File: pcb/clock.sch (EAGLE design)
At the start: 50 parts, among them K1 JS-M1-9V-4, K2 JS-M1-9V-4, Q1 BC447, Q2 BC447, Q3 BC447, Q4 BC447, Q5 BC447, Q6 BC447, Q8 CSM-7X-DU, Q9 MC-306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

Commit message: some small things
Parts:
- added C2: (no value), rcl:C-EUC1206
- added C7: (no value), rcl:C-EU025-040X050
- added D1: (no value), diode:DIODE-SOD80C
- added R23: (no value), rcl:R-EU_R1206
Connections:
- new net N$66: C2.2, U1.AREF
- new net N$67: D1.C, D2.C, R23.2
- new net N$68: R23.1, U2.VDD
- net GND: now also C2.1, C7.2
- net VCC: now also C7.1, D1.A, U1.AVCC; no longer D2.C, U2.VDD
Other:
- moved on the sheet: K1, K2, Q5, Q6, Q9, R19, R20, U2, X1-2, X2-1, X2-2, X2-3

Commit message: extend board
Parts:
- removed C4: (no value), rcl:C-EUC1206
- added C6: (no value), rcl:C-EUC0805K
- C3: device rcl:C-EUC1206 -> rcl:C-EUC0805K
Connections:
- net GND: now also C6.1; no longer C4.1
- net N$30: now also C6.2; no longer C3.2
- net N$31: now also C3.2; no longer C4.2
- net N$35: now also JP3.3
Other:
- moved on the sheet: C3
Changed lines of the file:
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@@
 <setting verticaltext="up"/>
 </settings>
-<grid distance="0.1" unitdist="inch" unit="inch" style="lines" multiple="1" display="no" altdistance="0.01" altunitdist="inch" altunit="inch"/>
+<grid distance="25" unitdist="mil" unit="mil" style="lines" multiple="1" display="no" altdistance="0.01" altunitdist="inch" altunit="inch"/>
 <layers>
 <layer number="1" name="Top" color="4" fill="1" visible="no" active="no"/>
@@
 <part name="SUPPLY10" library="supply2" deviceset="VCC" device=""/>
 <part name="U$1" library="display-kingbright" deviceset="4DIGITS-7SEGMENT-C" device=""/>
-<part name="C3" library="rcl" deviceset="C-EU" device="C1206"/>
-<part name="C4" library="rcl" deviceset="C-EU" device="C1206"/>
 <part name="GND6" library="supply1" deviceset="GND" device=""/>
 <part name="GND7" library="supply1" deviceset="GND" device=""/>
@@
 <part name="D1" library="diode" deviceset="DIODE-" device="SOD80C"/>
 <part name="R23" library="rcl" deviceset="R-EU_" device="R1206"/>
+<part name="C6" library="rcl" deviceset="C-EU" device="C0805K"/>
+<part name="C3" library="rcl" deviceset="C-EU" device="C0805K"/>
 </parts>
 <sheets>
@@
 <instance part="SUPPLY10" gate="G$1" x="106.045" y="121.285"/>
 <instance part="U$1" gate="A" x="215.9" y="99.06"/>
-<instance part="C3" gate="G$1" x="38.1" y="43.18" rot="R90"/>
-<instance part="C4" gate="G$1" x="38.1" y="38.1" rot="R90"/>
 <instance part="GND6" gate="1" x="35.56" y="27.94"/>
 <instance part="GND7" gate="1" x="145.415" y="-4.445"/>
@@
 <instance part="D1" gate="G$1" x="118.745" y="115.57" rot="R270"/>
 <instance part="R23" gate="G$1" x="131.445" y="109.855" rot="R180"/>
+<instance part="C6" gate="G$1" x="38.1" y="43.18" rot="R90"/>
+<instance part="C3" gate="G$1" x="38.1" y="38.1" rot="R90"/>
 </instances>
 <busses>
@@
 </segment>
 <segment>
-<pinref part="C3" gate="G$1" pin="1"/>
-<pinref part="C4" gate="G$1" pin="1"/>
-<wire x1="35.56" y1="43.18" x2="35.56" y2="38.1" width="0.1524" layer="91"/>
 <pinref part="GND6" gate="1" pin="GND"/>
 <wire x1="35.56" y1="30.48" x2="35.56" y2="38.1" width="0.1524" layer="91"/>
+<pinref part="C6" gate="G$1" pin="1"/>
+<pinref part="C3" gate="G$1" pin="1"/>
+<wire x1="35.56" y1="38.1" x2="35.56" y2="43.18" width="0.1524" layer="91"/>
 <junction x="35.56" y="38.1"/>
 </segment>
@@
 <pinref part="U1" gate="A" pin="PB6"/>
 <wire x1="48.26" y1="43.18" x2="45.085" y2="43.18" width="0.1524" layer="91"/>
-<pinref part="C3" gate="G$1" pin="2"/>
 <pinref part="Q8" gate="P" pin="2"/>
 <wire x1="45.085" y1="43.18" x2="43.18" y2="43.18" width="0.1524" layer="91"/>
 <junction x="45.085" y="43.18"/>
+<pinref part="C6" gate="G$1" pin="2"/>
 </segment>
 </net>
@@
 <wire x1="48.26" y1="40.64" x2="48.26" y2="38.1" width="0.1524" layer="91"/>
 <wire x1="48.26" y1="38.1" x2="45.085" y2="38.1" width="0.1524" layer="91"/>
-<pinref part="C4" gate="G$1" pin="2"/>
 <pinref part="Q8" gate="P" pin="1"/>
 <wire x1="45.085" y1="38.1" x2="43.18" y2="38.1" width="0.1524" layer="91"/>
 <junction x="45.085" y="38.1"/>
+<pinref part="C3" gate="G$1" pin="2"/>
 </segment>
 </net>
@@
 <pinref part="R7" gate="G$1" pin="1"/>
 <wire x1="137.795" y1="58.42" x2="167.64" y2="58.42" width="0.1524" layer="91"/>
-</segment>
-</net>
+<pinref part="JP3" gate="A" pin="3"/>
+<wire x1="118.745" y1="58.42" x2="137.795" y2="58.42" width="0.1524" layer="91"/>
+<junction x="137.795" y="58.42"/>
+</segment>
+</net>

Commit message: temp stable version
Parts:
- removed D1: (no value), diode:DIODE-SOD80C
- removed R23: (no value), rcl:R-EU_R1206
- added D3: ES2D, diode:ES2D
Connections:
- removed net N$68: R23.1, U2.VDD
- net N$67: now also D3.C, U2.VDD; no longer D1.C, R23.2
- net VCC: now also D3.A; no longer D1.A
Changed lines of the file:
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@@
 <part name="GND22" library="supply1" deviceset="GND" device=""/>
 <part name="C7" library="rcl" deviceset="C-EU" device="025-040X050"/>
-<part name="D1" library="diode" deviceset="DIODE-" device="SOD80C"/>
-<part name="R23" library="rcl" deviceset="R-EU_" device="R1206"/>
 <part name="C6" library="rcl" deviceset="C-EU" device="C0805K"/>
 <part name="C3" library="rcl" deviceset="C-EU" device="C0805K"/>
+<part name="D3" library="diode" deviceset="ES2D" device=""/>
 </parts>
 <sheets>
@@
 <instance part="GND22" gate="1" x="34.925" y="63.5" rot="R270"/>
 <instance part="C7" gate="G$1" x="40.64" y="73.66"/>
-<instance part="D1" gate="G$1" x="118.745" y="115.57" rot="R270"/>
-<instance part="R23" gate="G$1" x="131.445" y="109.855" rot="R180"/>
 <instance part="C6" gate="G$1" x="38.1" y="43.18" rot="R90"/>
 <instance part="C3" gate="G$1" x="38.1" y="38.1" rot="R90"/>
+<instance part="D3" gate="G$1" x="118.745" y="115.57" rot="R270"/>
 </instances>
 <busses>
@@
 <segment>
 <pinref part="SUPPLY6" gate="G$1" pin="VCC"/>
-<pinref part="D1" gate="G$1" pin="A"/>
 <wire x1="118.745" y1="118.11" x2="118.745" y2="118.745" width="0.1524" layer="91"/>
+<pinref part="D3" gate="G$1" pin="A"/>
 </segment>
 </net>
@@
 <wire x1="126.365" y1="109.855" x2="126.365" y2="113.03" width="0.1524" layer="91"/>
 <wire x1="118.745" y1="109.855" x2="126.365" y2="109.855" width="0.1524" layer="91"/>
-<pinref part="D1" gate="G$1" pin="C"/>
 <wire x1="118.745" y1="109.855" x2="118.745" y2="113.03" width="0.1524" layer="91"/>
-<pinref part="R23" gate="G$1" pin="2"/>
+<pinref part="D3" gate="G$1" pin="C"/>
+<pinref part="U2" gate="A" pin="VDD"/>
+<wire x1="126.365" y1="109.855" x2="144.145" y2="109.855" width="0.1524" layer="91"/>
 <junction x="126.365" y="109.855"/>
 </segment>
 </net>
-<net name="N$68" class="0">
-<segment>
-<pinref part="U2" gate="A" pin="VDD"/>
-<pinref part="R23" gate="G$1" pin="1"/>
-<wire x1="136.525" y1="109.855" x2="144.145" y2="109.855" width="0.1524" layer="91"/>
-</segment>
-</net>

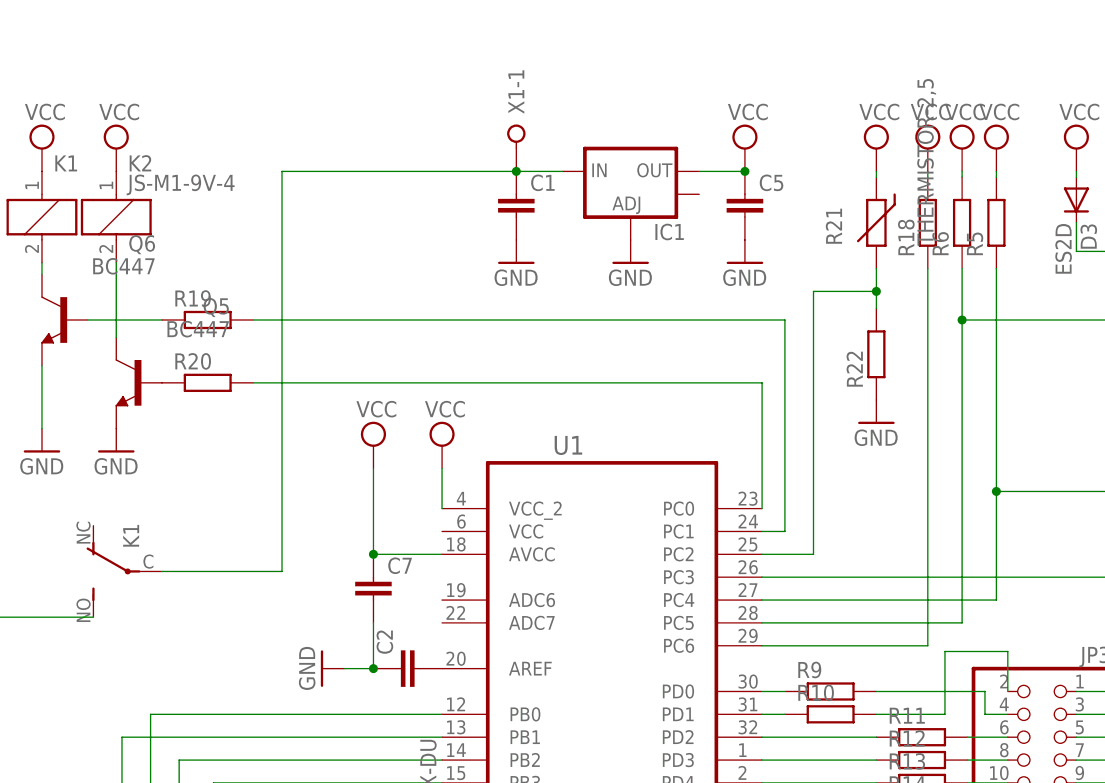
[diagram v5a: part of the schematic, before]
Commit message: board modification for use external device, move thermistor to adc6, software is not modificated yet
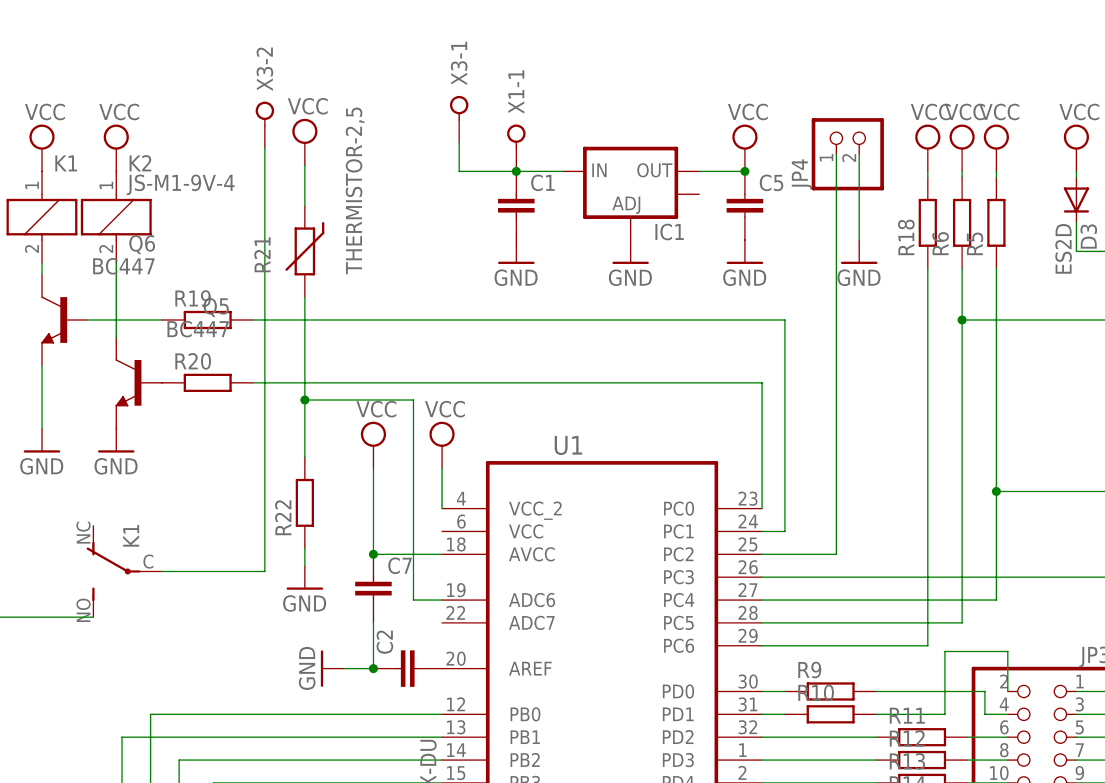
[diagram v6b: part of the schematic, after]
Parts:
- added JP4: (no value), pinhead:PINHD-1X2
- added X3: (no value), con-wago-508:W237-02P
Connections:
- new net N$68: JP4.1, U1.PC2
- new net N$73: C1.1, IC1.IN, X1-1.KL, X3-1.KL
- net GND: now also JP4.2
- net N$12: now also X3-2.KL; no longer C1.1, IC1.IN, X1-1.KL
- net N$36: now also U1.ADC6; no longer U1.PC2
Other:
- moved on the sheet: R21, R22
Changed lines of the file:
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@@
 <part name="C3" library="rcl" deviceset="C-EU" device="C0805K"/>
 <part name="D3" library="diode" deviceset="ES2D" device=""/>
+<part name="JP4" library="pinhead" deviceset="PINHD-1X2" device=""/>
+<part name="GND23" library="supply1" deviceset="GND" device=""/>
+<part name="X3" library="con-wago-508" deviceset="W237-02P" device=""/>
 </parts>
 <sheets>
@@
 <instance part="R3" gate="G$1" x="91.44" y="15.24"/>
 <instance part="R4" gate="G$1" x="91.44" y="20.955"/>
-<instance part="R21" gate="G$1" x="96.52" y="113.03" rot="R90"/>
-<instance part="R22" gate="G$1" x="96.52" y="98.425" rot="R90"/>
-<instance part="GND19" gate="1" x="96.52" y="90.805"/>
-<instance part="SUPPLY2" gate="G$1" x="96.52" y="121.285"/>
+<instance part="R21" gate="G$1" x="33.02" y="109.855" rot="R90"/>
+<instance part="R22" gate="G$1" x="33.02" y="81.915" rot="R90"/>
+<instance part="GND19" gate="1" x="33.02" y="72.39"/>
+<instance part="SUPPLY2" gate="G$1" x="33.02" y="121.92"/>
 <instance part="X2" gate="-1" x="-20.32" y="115.57"/>
 <instance part="X2" gate="-2" x="-13.335" y="92.075" rot="R270"/>
@@
 <instance part="C3" gate="G$1" x="38.1" y="38.1" rot="R90"/>
 <instance part="D3" gate="G$1" x="118.745" y="115.57" rot="R270"/>
+<instance part="JP4" gate="G$1" x="94.615" y="123.19" rot="R90"/>
+<instance part="GND23" gate="1" x="94.615" y="108.585"/>
+<instance part="X3" gate="-1" x="50.165" y="127" rot="R270"/>
+<instance part="X3" gate="-2" x="28.575" y="126.365" rot="R270"/>
 </instances>
 <busses>
@@
 <pinref part="SUPPLY2" gate="G$1" pin="VCC"/>
 <pinref part="R21" gate="G$1" pin="1"/>
-<wire x1="96.52" y1="118.11" x2="96.52" y2="118.745" width="0.1524" layer="91"/>
+<wire x1="33.02" y1="114.935" x2="33.02" y2="119.38" width="0.1524" layer="91"/>
 </segment>
 <segment>
@@
 <pinref part="R22" gate="G$1" pin="1"/>
 <pinref part="GND19" gate="1" pin="GND"/>
+<wire x1="33.02" y1="74.93" x2="33.02" y2="76.835" width="0.1524" layer="91"/>
 </segment>
 <segment>
@@
 <pinref part="C7" gate="G$1" pin="2"/>
 </segment>
+<segment>
+<pinref part="JP4" gate="G$1" pin="2"/>
+<pinref part="GND23" gate="1" pin="GND"/>
+<wire x1="94.615" y1="111.125" x2="94.615" y2="120.65" width="0.1524" layer="91"/>
+</segment>
 </net>
 <net name="N$12" class="0">
 <segment>
-<pinref part="IC1" gate="G$1" pin="IN"/>
-<wire x1="56.515" y1="118.745" x2="61.595" y2="118.745" width="0.1524" layer="91"/>
-<pinref part="X1" gate="-1" pin="KL"/>
-<junction x="56.515" y="118.745"/>
-<wire x1="56.515" y1="118.745" x2="30.48" y2="118.745" width="0.1524" layer="91"/>
-<wire x1="30.48" y1="118.745" x2="30.48" y2="74.295" width="0.1524" layer="91"/>
-<wire x1="30.48" y1="74.295" x2="17.145" y2="74.295" width="0.1524" layer="91"/>
+<wire x1="28.575" y1="121.285" x2="28.575" y2="74.295" width="0.1524" layer="91"/>
+<wire x1="28.575" y1="74.295" x2="17.145" y2="74.295" width="0.1524" layer="91"/>
 <pinref part="K1" gate="2" pin="P"/>
-<pinref part="C1" gate="G$1" pin="1"/>
+<pinref part="X3" gate="-2" pin="KL"/>
 </segment>
 </net>
@@
 <pinref part="R22" gate="G$1" pin="2"/>
 <pinref part="R21" gate="G$1" pin="2"/>
-<wire x1="96.52" y1="107.95" x2="96.52" y2="105.41" width="0.1524" layer="91"/>
-<wire x1="96.52" y1="105.41" x2="96.52" y2="103.505" width="0.1524" layer="91"/>
-<wire x1="96.52" y1="105.41" x2="89.535" y2="105.41" width="0.1524" layer="91"/>
-<wire x1="89.535" y1="105.41" x2="89.535" y2="76.2" width="0.1524" layer="91"/>
-<pinref part="U1" gate="A" pin="PC2"/>
-<wire x1="89.535" y1="76.2" x2="83.82" y2="76.2" width="0.1524" layer="91"/>
-<junction x="96.52" y="105.41"/>
+<wire x1="33.02" y1="104.775" x2="33.02" y2="93.345" width="0.1524" layer="91"/>
+<wire x1="33.02" y1="93.345" x2="33.02" y2="86.995" width="0.1524" layer="91"/>
+<wire x1="33.02" y1="93.345" x2="45.085" y2="93.345" width="0.1524" layer="91"/>
+<wire x1="45.085" y1="93.345" x2="45.085" y2="71.12" width="0.1524" layer="91"/>
+<pinref part="U1" gate="A" pin="ADC6"/>
+<wire x1="45.085" y1="71.12" x2="48.26" y2="71.12" width="0.1524" layer="91"/>
+<junction x="33.02" y="93.345"/>
 </segment>
 </net>
@@
 </segment>
 </net>
+<net name="N$68" class="0">
+<segment>
+<pinref part="U1" gate="A" pin="PC2"/>
+<pinref part="JP4" gate="G$1" pin="1"/>
+<wire x1="83.82" y1="76.2" x2="92.075" y2="76.2" width="0.1524" layer="91"/>
+<wire x1="92.075" y1="76.2" x2="92.075" y2="120.65" width="0.1524" layer="91"/>
+</segment>
+</net>
+<net name="N$73" class="0">
+<segment>
+<pinref part="IC1" gate="G$1" pin="IN"/>
+<wire x1="56.515" y1="118.745" x2="61.595" y2="118.745" width="0.1524" layer="91"/>
+<pinref part="X1" gate="-1" pin="KL"/>
+<junction x="56.515" y="118.745"/>
+<pinref part="C1" gate="G$1" pin="1"/>
+<pinref part="X3" gate="-1" pin="KL"/>
+<wire x1="50.165" y1="121.92" x2="50.165" y2="118.745" width="0.1524" layer="91"/>
+<wire x1="50.165" y1="118.745" x2="56.515" y2="118.745" width="0.1524" layer="91"/>
+</segment>
+</net>
